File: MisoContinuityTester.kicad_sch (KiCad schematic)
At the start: 12 parts, among them J10 OUTPUT, J11 OUTPUT, J3 POWER SWITCH, J4 INPUT, J5 INPUT, J6 FAIL, J7 PASS, J8 POWER 5V-12V, J9 START

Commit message: added 3d models, worked on pcb
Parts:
- added J12: TYPE1, TerminalBlock_Phoenix:TerminalBlock_Phoenix_MPT-0,5-2-2.54_1x02_P2.54mm_Horizontal, symbol Connector:Screw_Terminal_01x02
- added J13: TYPE2, TerminalBlock_Phoenix:TerminalBlock_Phoenix_MPT-0,5-2-2.54_1x02_P2.54mm_Horizontal, symbol Connector:Screw_Terminal_01x02
- J10, J11, J4, J5: footprint (none) -> TerminalBlock:TerminalBlock_Xinya_XY308-2.54-10P_1x10_P2.54mm_Horizontal
- J3, J6, J7, J8, J9: footprint (none) -> TerminalBlock_Phoenix:TerminalBlock_Phoenix_MPT-0,5-2-2.54_1x02_P2.54mm_Horizontal
- U1, U2: footprint (none) -> addedItems:Adafruit MCP23017
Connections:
- net +5V: now also U1.26 (VIN), U2.26 (VIN), U2.3 (D0); no longer U1. (A7), U2. (A7)
- net A1: now also U1.21 (A0); no longer U1. (A7)
- net A10: now also U1.7 (B6); no longer U1. (A7)
- net A11: now also U1.8 (B5); no longer U1. (A7)
- net A12: now also U1.9 (B4); no longer U1. (A7)
- net A13: now also U1.10 (B3); no longer U1. (A7)
- net A14: now also U1.11 (B2); no longer U1. (A7)
- net A15: now also U1.12 (B1); no longer U1. (A7)
- net A16: now also U1.13 (B0); no longer U1. (A7)
- net A17: now also U2.21 (A0); no longer U2. (A7)
- net A18: now also U2.20 (A1); no longer U2. (A7)
- net A19: now also U2.19 (A2); no longer U2. (A7)
- net A2: now also U1.20 (A1); no longer U1. (A7)
- net A20: now also U2.18 (A3); no longer U2. (A7)
- net A3: now also U1.19 (A2); no longer U1. (A7)
- net A4: now also U1.18 (A3); no longer U1. (A7)
- net A5: now also U1.17 (A4); no longer U1. (A7)
- net A6: now also U1.16 (A5); no longer U1. (A7)
- net A7: now also U1.15 (A6); no longer U1. (A7)
- net A8: now also U1.14 (A7); no longer U1. (A7)
- net A9: now also U1.6 (B7); no longer U1. (A7)
- net B1: now also U2.17 (A4); no longer U2. (A7)
- net B10: now also U2.11 (B2); no longer U2. (A7)
- net B11: now also U2.12 (B1); no longer U2. (A7)
- net B12: now also U2.13 (B0); no longer U2. (A7)
- net B2: now also U2.16 (A5); no longer U2. (A7)
- net B3: now also U2.15 (A6); no longer U2. (A7)
- net B4: now also U2.14 (A7); no longer U2. (A7)
- net B5: now also U2.6 (B7); no longer U2. (A7)
- net B6: now also U2.7 (B6); no longer U2. (A7)
- net B7: now also U2.8 (B5); no longer U2. (A7)
- net B8: now also U2.9 (B4); no longer U2. (A7)
- net B9: now also U2.10 (B3); no longer U2. (A7)
- net GND: now also U1.25 (GND), U1.3 (D0), U1.4 (D1), U1.5 (D2), U2.25 (GND), U2.4 (D1), U2.5 (D2), J13.1 (Pin_1); no longer U1. (A7), U2. (A7)
- net 9-WIRE: now reaches A1.21 (A2)
- net 9-WIRE: now also J12.2 (Pin_2)
- net 18-WIRE: now reaches A1.22 (A3)
- net 18-WIRE: now also J12.1 (Pin_1)
- net 20-WIRE: now reaches A1.23 (SDA/A4)
- net 20-WIRE: now also J13.2 (Pin_2)
- new net: U1.23 (SDA), U2.23 (SDA)
- new net: U1.24 (SCL), U2.24 (SCL)
- no-connect marks 20 -> 17
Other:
- moved on the sheet: J3, J8

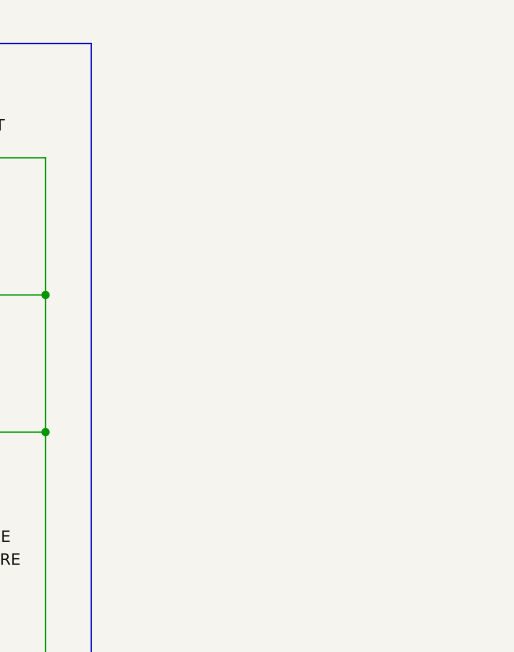
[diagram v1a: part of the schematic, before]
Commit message: added mounting holes
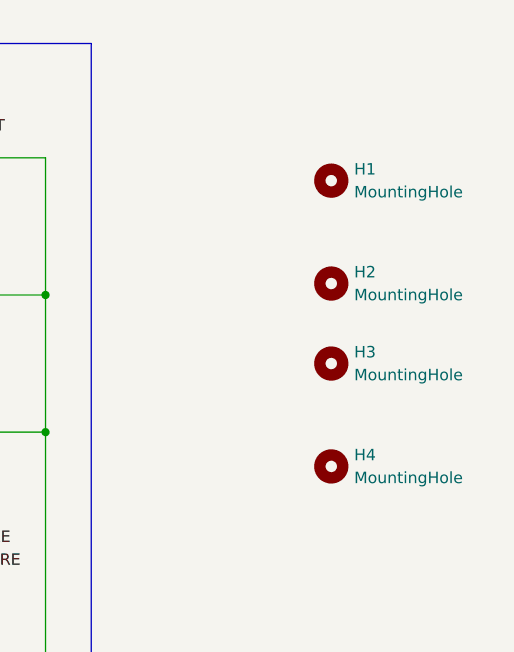
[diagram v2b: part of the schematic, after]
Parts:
- added H1, H2, H3, H4: MountingHole, MountingHole:MountingHole_4.3mm_M4, symbol Mechanical:MountingHole

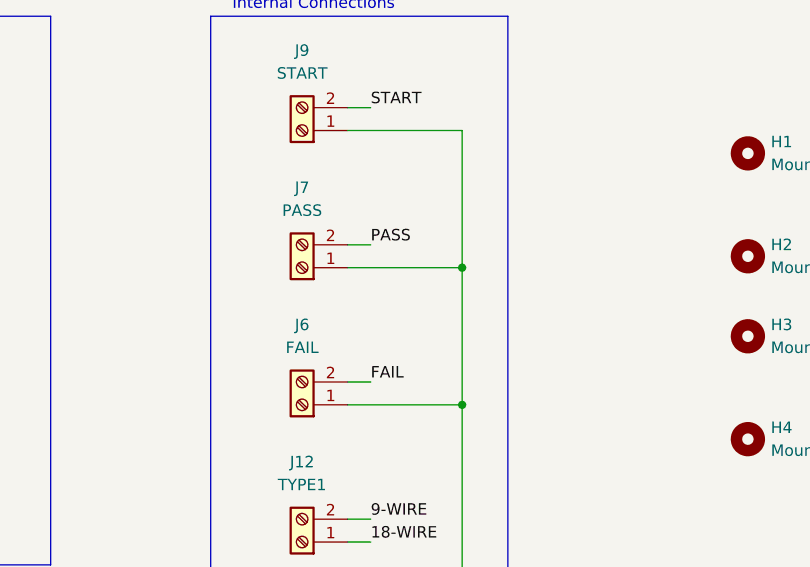
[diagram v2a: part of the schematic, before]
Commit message: wired everything up and added resistors for pass and fail
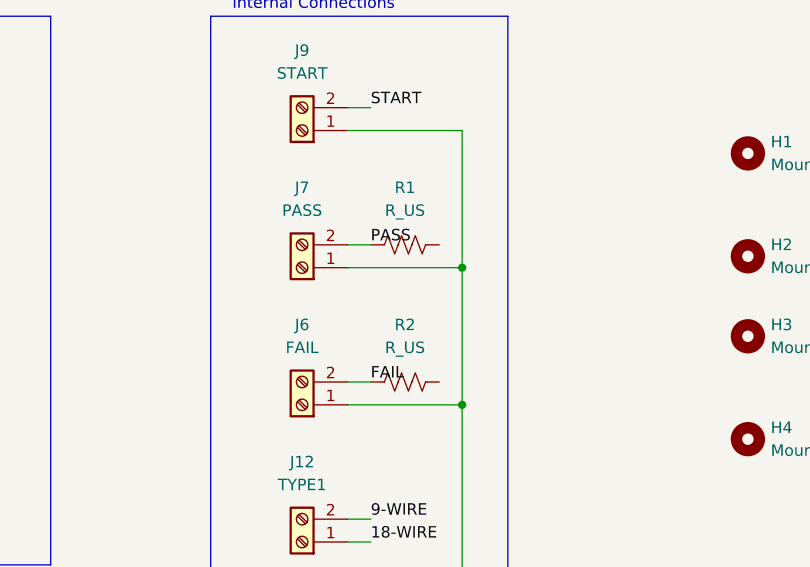
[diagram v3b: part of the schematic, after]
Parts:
- added R1, R2: R_US, Resistor_THT:R_Axial_DIN0204_L3.6mm_D1.6mm_P5.08mm_Horizontal, symbol Device:R_US
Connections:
- net FAIL: now also R2.1
- net PASS: now also R1.1
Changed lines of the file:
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@@
+	)
+	(symbol
+		(lib_id "Device:R_US")
+		(at 226.06 46.99 90)
+		(unit 1)
+		(exclude_from_sim no)
+		(in_bom yes)
+		(on_board yes)
+		(dnp no)
+		(fields_autoplaced yes)
+		(property "Reference" "R1"
+			(at 226.06 40.64 90)
+			(effects
+				(font
+					(size 1.27 1.27)
+				)
+			)
+		)
+		(property "Value" "R_US"
+			(at 226.06 43.18 90)
+			(effects
+				(font
+					(size 1.27 1.27)
+				)
+			)
+		)
+		(property "Footprint" "Resistor_THT:R_Axial_DIN0204_L3.6mm_D1.6mm_P5.08mm_Horizontal"
+			(at 226.314 45.974 90)
+			(effects
+				(font
+					(size 1.27 1.27)
+				)
+				(hide yes)
+			)
+		)
+		(property "Datasheet" "~"
+			(at 226.06 46.99 0)
+			(effects
+				(font
+					(size 1.27 1.27)
+				)
+				(hide yes)
+			)
+		)
+		(property "Description" "Resistor, US symbol"
+			(at 226.06 46.99 0)
+			(effects
+				(font
+					(size 1.27 1.27)
+				)
+				(hide yes)
+			)
+		)
+		(pin "1"
+		)
+		(pin "2"
+		)
+		(instances
+			(project ""
+				(path "/0d35483a-0b12-46cc-b9f2-896fd6831779"
+					(reference "R1")
+					(unit 1)
+				)
+			)
+		)
+	)
+	(symbol
+		(lib_id "Device:R_US")
+		(at 226.06 62.23 90)
+		(unit 1)
+		(exclude_from_sim no)
+		(in_bom yes)
+		(on_board yes)
+		(dnp no)
+		(fields_autoplaced yes)
+		(property "Reference" "R2"
+			(at 226.06 55.88 90)
+			(effects
+				(font
+					(size 1.27 1.27)
+				)
+			)
+		)
+		(property "Value" "R_US"
+			(at 226.06 58.42 90)
+			(effects
+				(font
+					(size 1.27 1.27)
+				)
+			)
+		)
+		(property "Footprint" "Resistor_THT:R_Axial_DIN0204_L3.6mm_D1.6mm_P5.08mm_Horizontal"
+			(at 226.314 61.214 90)
+			(effects
+				(font
+					(size 1.27 1.27)
+				)
+				(hide yes)
+			)
+		)
+		(property "Datasheet" "~"
+			(at 226.06 62.23 0)
+			(effects
+				(font
+					(size 1.27 1.27)
+				)
+				(hide yes)
+			)
+		)
+		(property "Description" "Resistor, US symbol"
+			(at 226.06 62.23 0)
+			(effects
+				(font
+					(size 1.27 1.27)
+				)
+				(hide yes)
+			)
+		)
+		(pin "1"
+		)
+		(pin "2"
+		)
+		(instances
+			(project ""
+				(path "/0d35483a-0b12-46cc-b9f2-896fd6831779"
+					(reference "R2")
+					(unit 1)
+				)
+			)
+		)
 	)
 	(symbol

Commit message: See OneDrive notes - IB
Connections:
- net FAIL: now also R2.2; no longer J6.2 (Pin_2), R2.1
- net PASS: now also R1.2; no longer J7.2 (Pin_2), R1.1
- new net: J6.2 (Pin_2), R2.1
- new net: J7.2 (Pin_2), R1.1
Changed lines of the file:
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@@
 	(rectangle
 		(start 204.47 21.59)
-		(end 237.49 113.03)
+		(end 241.3 113.03)
 		(stroke
 			(width 0)
@@
 	(wire
 		(pts
+			(xy 234.95 46.99) (xy 229.87 46.99)
+		)
+		(stroke
+			(width 0)
+			(type default)
+		)
+	)
+	(wire
+		(pts
 			(xy 55.88 132.08) (xy 58.42 132.08)
 		)
@@
 		(pts
 			(xy 81.28 67.31) (xy 85.09 67.31)
+		)
+		(stroke
+			(width 0)
+			(type default)
+		)
+	)
+	(wire
+		(pts
+			(xy 234.95 62.23) (xy 229.87 62.23)
 		)
 		(stroke
@@
 		)
 	)
-	(label "FAIL"
-		(at 222.25 62.23 0)
-		(effects
-			(font
-				(size 1.27 1.27)
-			)
-			(justify left bottom)
-		)
-	)
 	(label "B1"
 		(at 86.36 176.53 0)
@@
 		)
 	)
+	(label "FAIL"
+		(at 234.95 62.23 0)
+		(effects
+			(font
+				(size 1.27 1.27)
+			)
+			(justify left bottom)
+		)
+	)
 	(label "A19"
 		(at 140.97 30.48 0)
@@
 		)
 	)
+	(label "PASS"
+		(at 234.95 46.99 0)
+		(effects
+			(font
+				(size 1.27 1.27)
+			)
+			(justify left bottom)
+		)
+	)
 	(label "START"
 		(at 222.25 31.75 0)
@@
 		(effects
 			(font
-				(size 1.27 1.27)
-			)
-			(justify left bottom)
-		)
-	)
-	(label "PASS"
-		(at 222.25 46.99 0)
-		(effects
-			(font

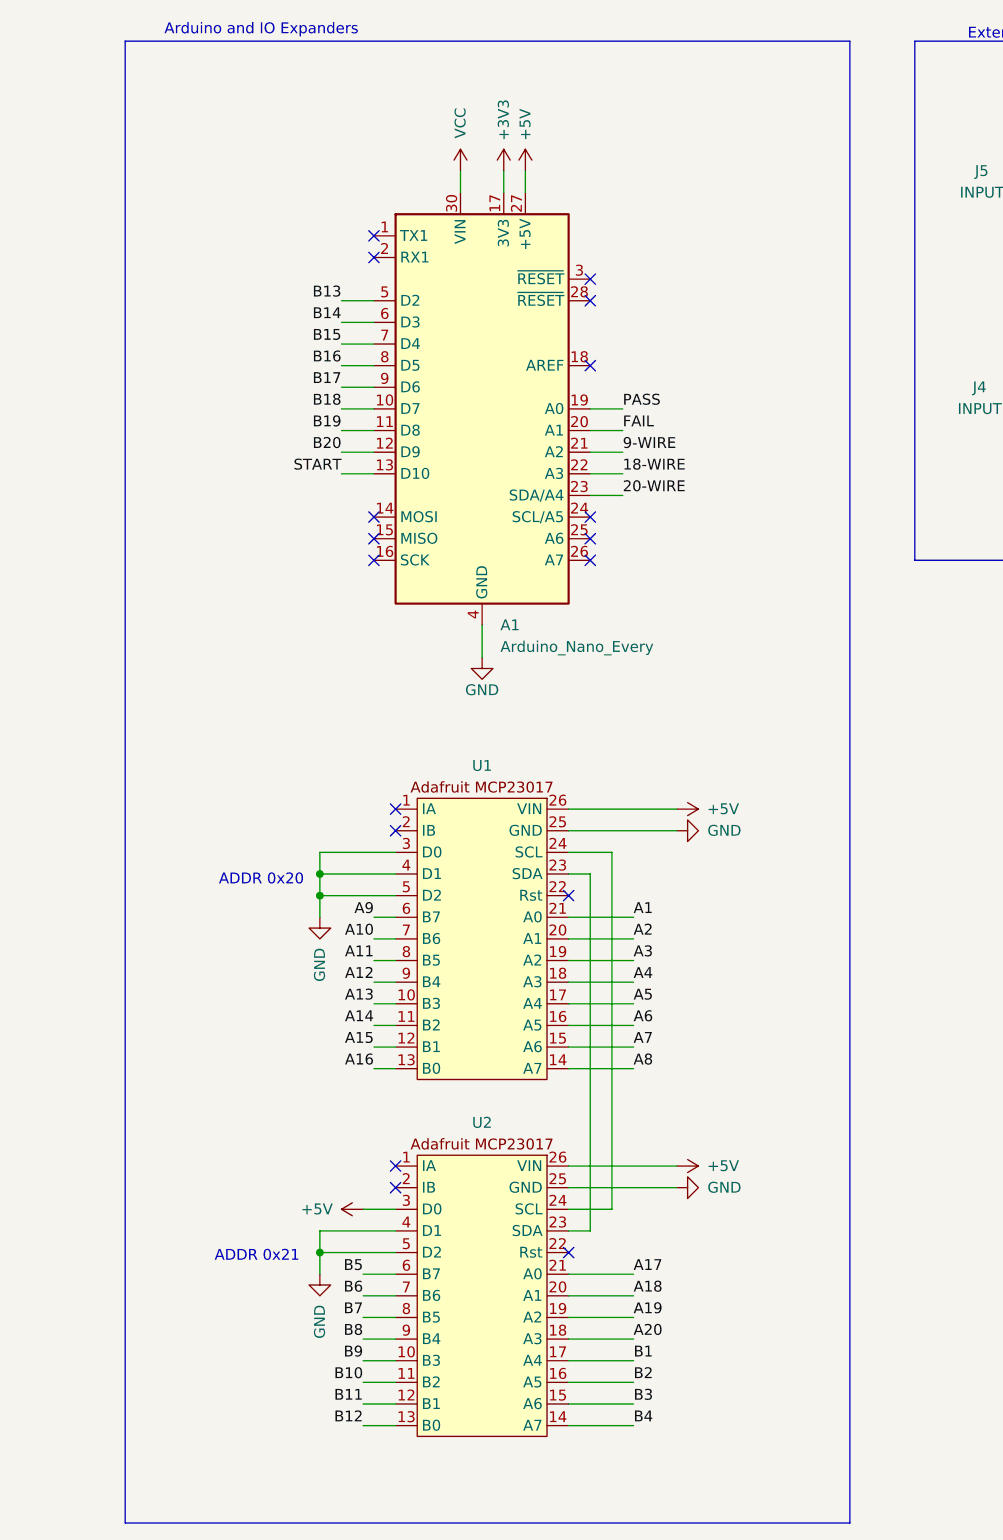
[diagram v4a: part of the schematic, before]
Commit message: connected adress pins from Exp 1 and 2 to NANO, changed around where the switchs all go
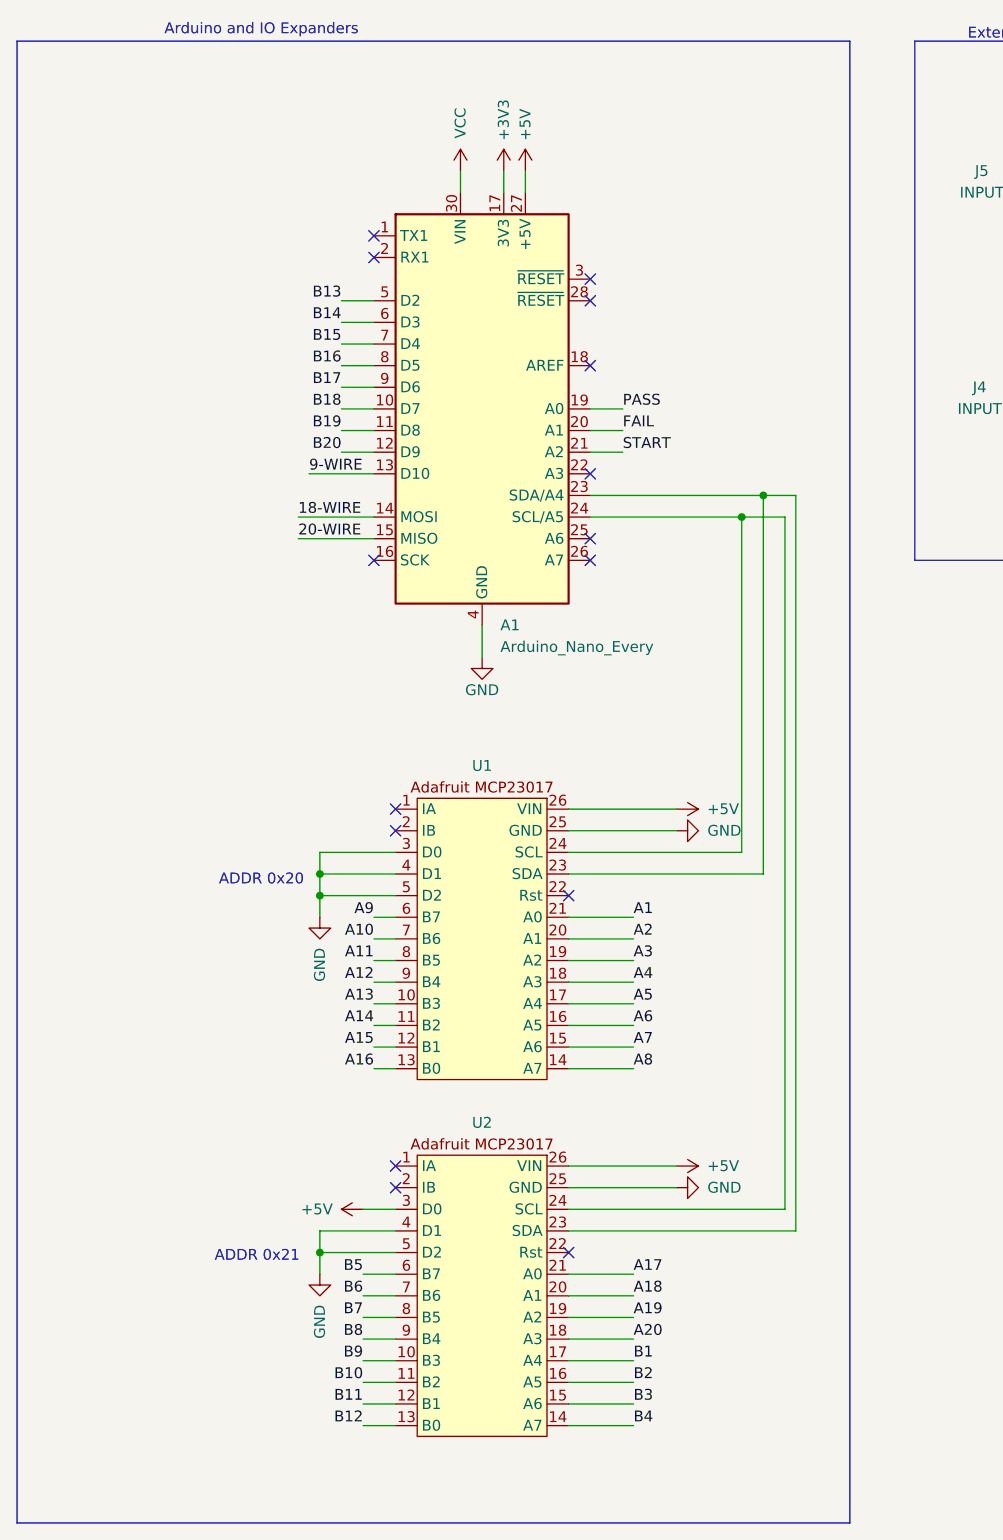
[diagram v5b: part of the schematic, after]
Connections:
- net 18-WIRE: now also A1.14 (MOSI); no longer A1.22 (A3)
- net 20-WIRE: now also A1.15 (MISO); no longer A1.23 (SDA/A4)
- net 9-WIRE: now also A1.13 (D10); no longer A1.21 (A2)
- net START: now also A1.21 (A2); no longer A1.13 (D10)
- net at U1.23 (SDA), U2.23 (SDA): now also A1.23 (SDA/A4)
- net at U1.24 (SCL), U2.24 (SCL): now also A1.24 (SCL/A5)
- no-connect marks 17 -> 15
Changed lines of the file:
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@@
 	)
 	(rectangle
-		(start 26.67 21.59)
+		(start 13.97 21.59)
 		(end 111.76 195.58)
 		(stroke
@@
 			)
 		)
+	)
+	(junction
+		(at 99.06 77.47)
+		(diameter 0)
+		(color 0 0 0 0)
 	)
 	(junction
@@
 		(color 0 0 0 0)
 	)
+	(junction
+		(at 101.6 74.93)
+		(diameter 0)
+		(color 0 0 0 0)
+	)
 	(no_connect
 		(at 81.28 49.53)
@@
 	)
 	(no_connect
-		(at 55.88 77.47)
+		(at 78.74 163.83)
 	)
 	(no_connect
-		(at 78.74 163.83)
+		(at 55.88 82.55)
 	)
 	(no_connect
@@
 	)
 	(no_connect
+		(at 81.28 72.39)
+	)
+	(no_connect
 		(at 58.42 156.21)
-	)
-	(no_connect
-		(at 55.88 82.55)
 	)
 	(no_connect
@@
 	)
 	(no_connect
-		(at 81.28 77.47)
-	)
-	(no_connect
 		(at 58.42 114.3)
 	)
@@
 		(at 78.74 121.92)
 	)
-	(no_connect
-		(at 55.88 80.01)
-	)
 	(wire
 		(pts
@@
 	(wire
 		(pts
-			(xy 85.09 74.93) (xy 81.28 74.93)
-		)
-		(stroke
-			(width 0)
-			(type default)
-		)
-	)
-	(wire
-		(pts
-			(xy 85.09 72.39) (xy 81.28 72.39)
-		)
-		(stroke
-			(width 0)
-			(type default)
-		)
-	)
-	(wire
-		(pts
 			(xy 137.16 50.8) (xy 140.97 50.8)
 		)
@@
 	(wire
 		(pts
-			(xy 78.74 116.84) (xy 83.82 116.84)
+			(xy 104.14 77.47) (xy 99.06 77.47)
+		)
+		(stroke
+			(width 0)
+			(type default)
+		)
+	)
+	(wire
+		(pts
+			(xy 78.74 116.84) (xy 99.06 116.84)
 		)
 		(stroke
@@
 	(wire
 		(pts
-			(xy 81.28 119.38) (xy 81.28 161.29)
-		)
-		(stroke
-			(width 0)
-			(type default)
-		)
-	)
-	(wire
-		(pts
 			(xy 137.16 35.56) (xy 140.97 35.56)
 		)
@@
 	(wire
 		(pts
-			(xy 83.82 158.75) (xy 78.74 158.75)
+			(xy 78.74 158.75) (xy 104.14 158.75)
 		)
 		(stroke
@@
 	(wire
 		(pts
+			(xy 101.6 74.93) (xy 101.6 119.38)
+		)
+		(stroke
+			(width 0)
+			(type default)
+		)
+	)
+	(wire
+		(pts
 			(xy 170.18 40.64) (xy 173.99 40.64)
 		)
@@
 	(wire
 		(pts
-			(xy 81.28 161.29) (xy 78.74 161.29)
+			(xy 78.74 161.29) (xy 105.41 161.29)
+		)
+		(stroke
+			(width 0)
+			(type default)
+		)
+	)
+	(wire
+		(pts
+			(xy 99.06 77.47) (xy 99.06 116.84)
 		)
 		(stroke
@@
 	(wire
 		(pts
-			(xy 52.07 72.39) (xy 55.88 72.39)
-		)
-		(stroke
-			(width 0)
-			(type default)
-		)
-	)
-	(wire
-		(pts
 			(xy 52.07 52.07) (xy 55.88 52.07)
 		)
@@
 	(wire
 		(pts
+			(xy 81.28 77.47) (xy 99.06 77.47)
+		)
+		(stroke
+			(width 0)
+			(type default)
+		)
+	)
+	(wire
+		(pts
 			(xy 66.04 36.83) (xy 66.04 39.37)
 		)
@@
 	(wire
 		(pts
-			(xy 78.74 119.38) (xy 81.28 119.38)
+			(xy 78.74 119.38) (xy 101.6 119.38)
 		)
 		(stroke
@@
 	(wire
 		(pts
+			(xy 81.28 69.85) (xy 85.09 69.85)
+		)
+		(stroke
+			(width 0)
+			(type default)
+		)
+	)
+	(wire
+		(pts
 			(xy 170.18 68.58) (xy 173.99 68.58)
 		)
@@
 	(wire
 		(pts
+			(xy 105.41 74.93) (xy 101.6 74.93)
+		)
+		(stroke
+			(width 0)
+			(type default)
+		)
+	)
+	(wire
+		(pts
+			(xy 48.26 72.39) (xy 55.88 72.39)
+		)
+		(stroke
+			(width 0)
+			(type default)
+		)
+	)
+	(wire
+		(pts
 			(xy 78.74 111.76) (xy 91.44 111.76)
 		)
@@
 	(wire
 		(pts
+			(xy 46.99 77.47) (xy 55.88 77.47)
+		)
+		(stroke
+			(width 0)
+			(type default)
+		)
+	)
+	(wire
+		(pts
 			(xy 137.16 58.42) (xy 140.97 58.42)
 		)
@@
 	(wire
 		(pts
-			(xy 85.09 69.85) (xy 81.28 69.85)
-		)
-		(stroke
-			(width 0)
-			(type default)
-		)
-	)
-	(wire
-		(pts
 			(xy 78.74 142.24) (xy 86.36 142.24)
 		)
@@
 	(wire
 		(pts
+			(xy 46.99 80.01) (xy 55.88 80.01)
+		)
+		(stroke
+			(width 0)
+			(type default)
+		)
+	)
+	(wire
+		(pts
 			(xy 54.61 173.99) (xy 58.42 173.99)
 		)
@@
 	(wire
 		(pts
-			(xy 83.82 116.84) (xy 83.82 158.75)
+			(xy 105.41 161.29) (xy 105.41 74.93)
+		)
+		(stroke
+			(width 0)
+			(type default)
+		)
+	)
+	(wire
+		(pts
+			(xy 81.28 74.93) (xy 101.6 74.93)
+		)
+		(stroke
+			(width 0)
+			(type default)
+		)
+	)
+	(wire
+		(pts
+			(xy 104.14 158.75) (xy 104.14 77.47)
 		)
 		(stroke
@@
 		)
 	)
-	(label "18-WIRE"
-		(at 85.09 72.39 0)
-		(effects
-			(font
-				(size 1.27 1.27)
-			)
-			(justify left bottom)
-		)
-	)
 	(label "A18"
 		(at 86.36 168.91 0)
@@
 		)
 	)
-	(label "9-WIRE"
-		(at 85.09 69.85 0)
-		(effects
-			(font
-				(size 1.27 1.27)
-			)
-			(justify left bottom)
-		)
-	)
 	(label "A4"
 		(at 140.97 68.58 0)
@@
 		)
 	)
+	(label "START"
+		(at 85.09 69.85 0)
+		(effects
+			(font
+				(size 1.27 1.27)
+			)
+			(justify left bottom)
+		)
+	)
 	(label "B6"
 		(at 54.61 168.91 180)
@@
 		)
 	)
+	(label "9-WIRE"
+		(at 48.26 72.39 0)
+		(effects
+			(font
+				(size 1.27 1.27)
+			)
+			(justify left bottom)
+		)
+	)
 	(label "B5"
 		(at 173.99 66.04 0)
@@
 		)
 	)
-	(label "20-WIRE"
-		(at 85.09 74.93 0)
-		(effects
-			(font
-				(size 1.27 1.27)
-			)
-			(justify left bottom)
-		)
-	)
 	(label "B11"
 		(at 173.99 50.8 0)
@@
 		)
 	)
+	(label "18-WIRE"
+		(at 46.99 77.47 0)
+		(effects
+			(font
+				(size 1.27 1.27)
+			)
+			(justify left bottom)
+		)
+	)
+	(label "20-WIRE"
+		(at 46.99 80.01 0)
+		(effects
+			(font
+				(size 1.27 1.27)
+			)
+			(justify left bottom)
+		)
+	)
 	(label "B4"
 		(at 173.99 68.58 0)
@@
 		(effects
 			(font
-				(size 1.27 1.27)
-			)
-			(justify right bottom)
-		)
-	)
-	(label "START"
-		(at 52.07 72.39 180)
-		(effects
-			(font
